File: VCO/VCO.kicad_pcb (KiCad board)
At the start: 2 copper layers, 37 x 113.9 mm, 106 parts, among them J1 SYNC, J10 SQR, J2 PWM, J3 LIN, J4 CV1, J5 CV2, J6 CV3, J7 SIN, J8 TRI, J9 RMP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

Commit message: Add files via upload
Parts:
- removed G***: LOGO, graphics:errata logo
- removed G***: LOGO, graphics:logo_openhardware

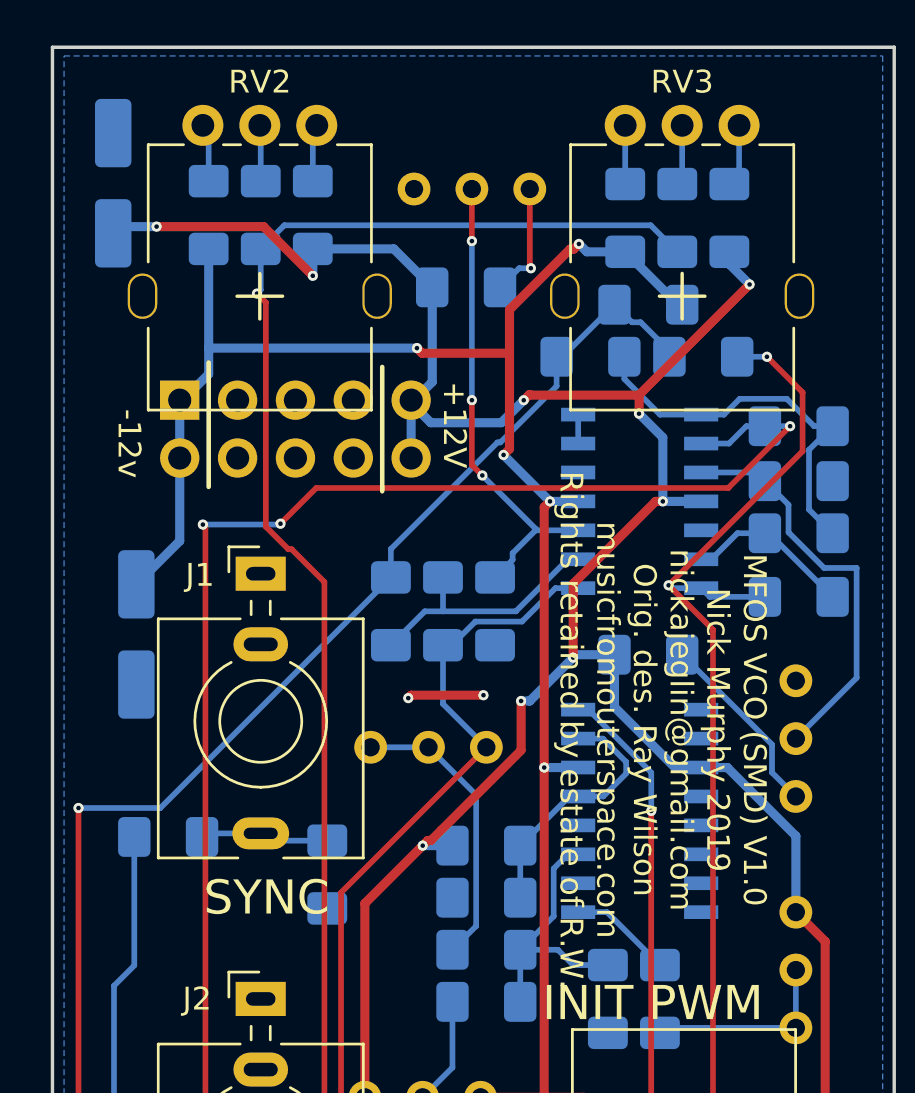
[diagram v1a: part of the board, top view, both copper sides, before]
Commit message: Add files via upload
Fixed reversed pot leads and C12 silk polarity. Cleaned up some power routing.
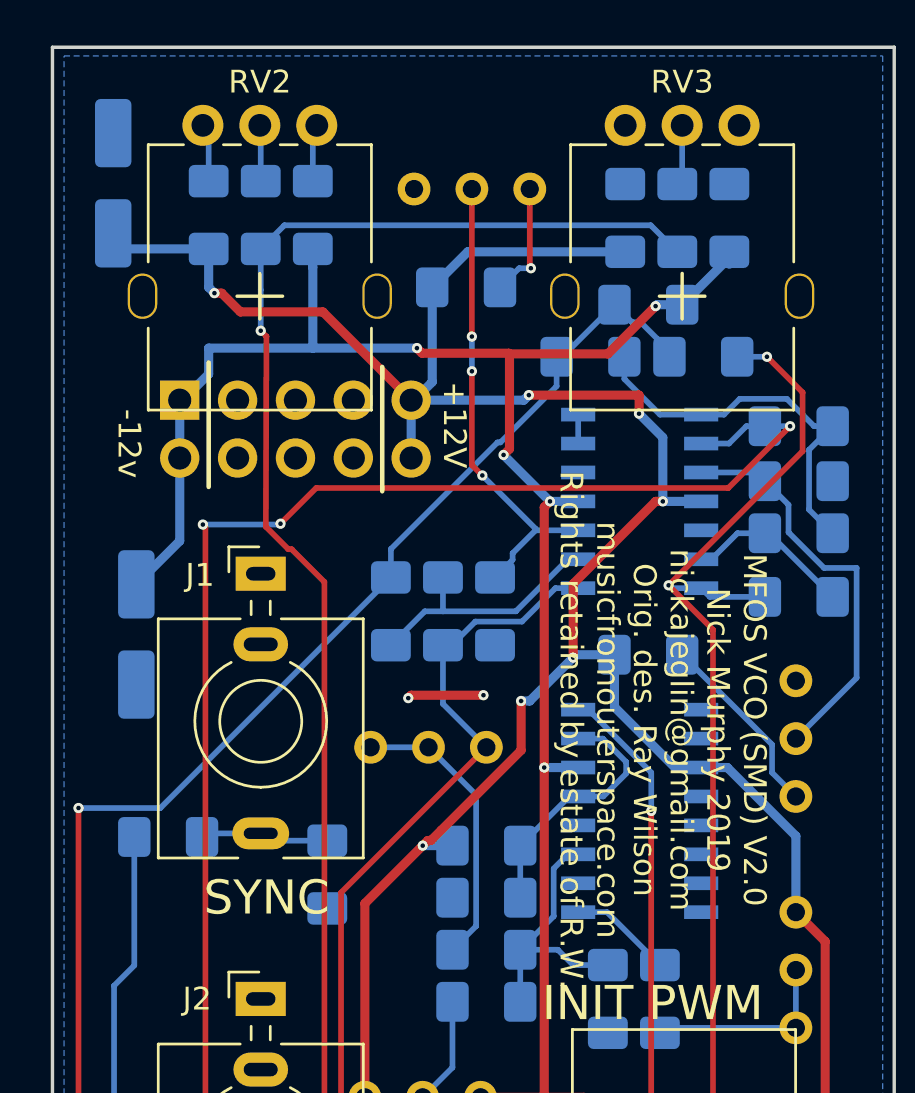
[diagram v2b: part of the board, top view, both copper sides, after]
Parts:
- moved R56 4.57 mm to (174.0, -204.6)
- moved R57 4.57 mm to (169.4, -204.6)
- moved R65 4.57 mm to (151.1, -204.7)
- moved R71 4.57 mm to (155.7, -204.7)
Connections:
- RV2 pad 1: R2P1 -> R2P3
- RV2 pad 3: R2P3 -> R2P1
- RV3 pad 1: R3P1 -> R3P3
- RV3 pad 3: R3P3 -> R3P1
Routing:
- net R3P3: track 2.75 -> 0.00 mm
- net R3P1: track 2.58 -> 0.61 mm
- net -12V: track 183.8 -> 184.8 mm
- net +12V: track 237.1 -> 237.2 mm, vias 17 -> 15
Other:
- board text added: "MFOS VCO (SMD) V2.0 Nick Murphy 2019 nickajeglin@gmail.com Orig. des. Ray Wilson musicfromouterspace.com Rights retained by estate of R.W."
- board text removed: "MFOS VCO (SMD) V1.0 Nick Murphy 2019 nickajeglin@gmail.com Orig. des. Ray Wilson musicfromouterspace.com Rights retained by estate of R.W."
